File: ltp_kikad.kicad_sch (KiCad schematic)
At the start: 17 parts, among them IC1 SamacSys_Parts_HT16K33-28SOP, IC2 SamacSys_Parts_HT16K33-28SOP, J2 RPi_GPIO

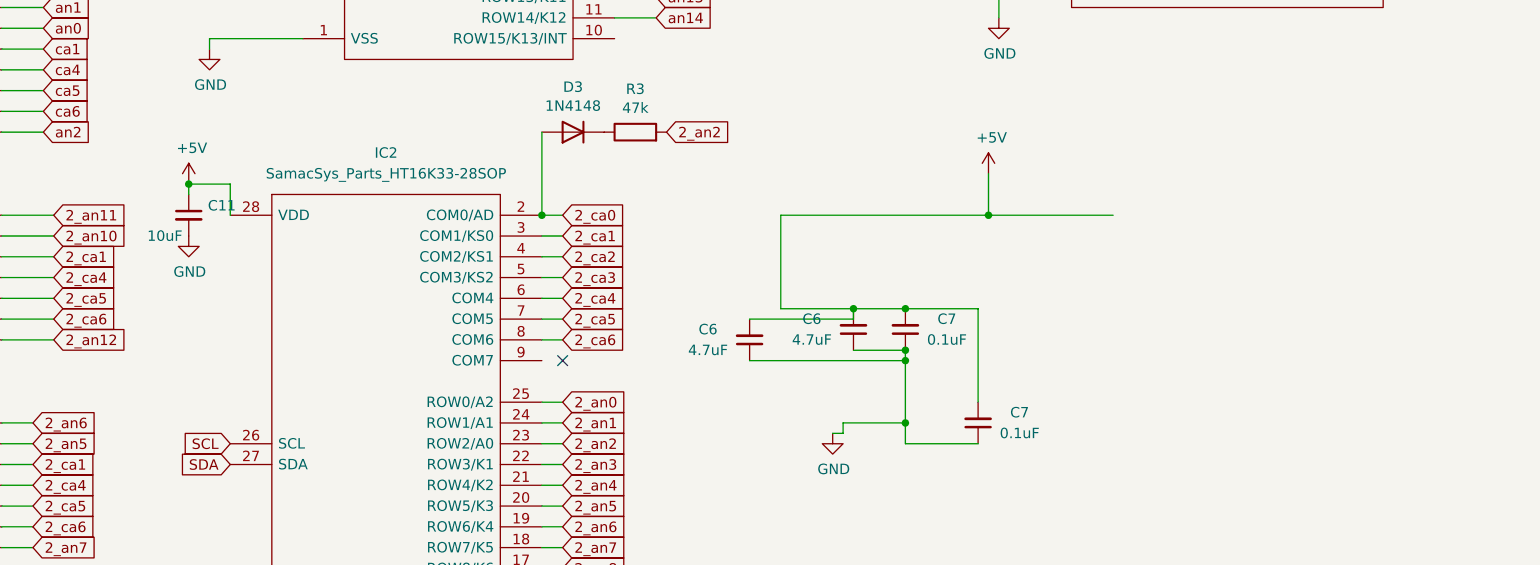
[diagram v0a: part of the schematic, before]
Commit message: Add bypas cap
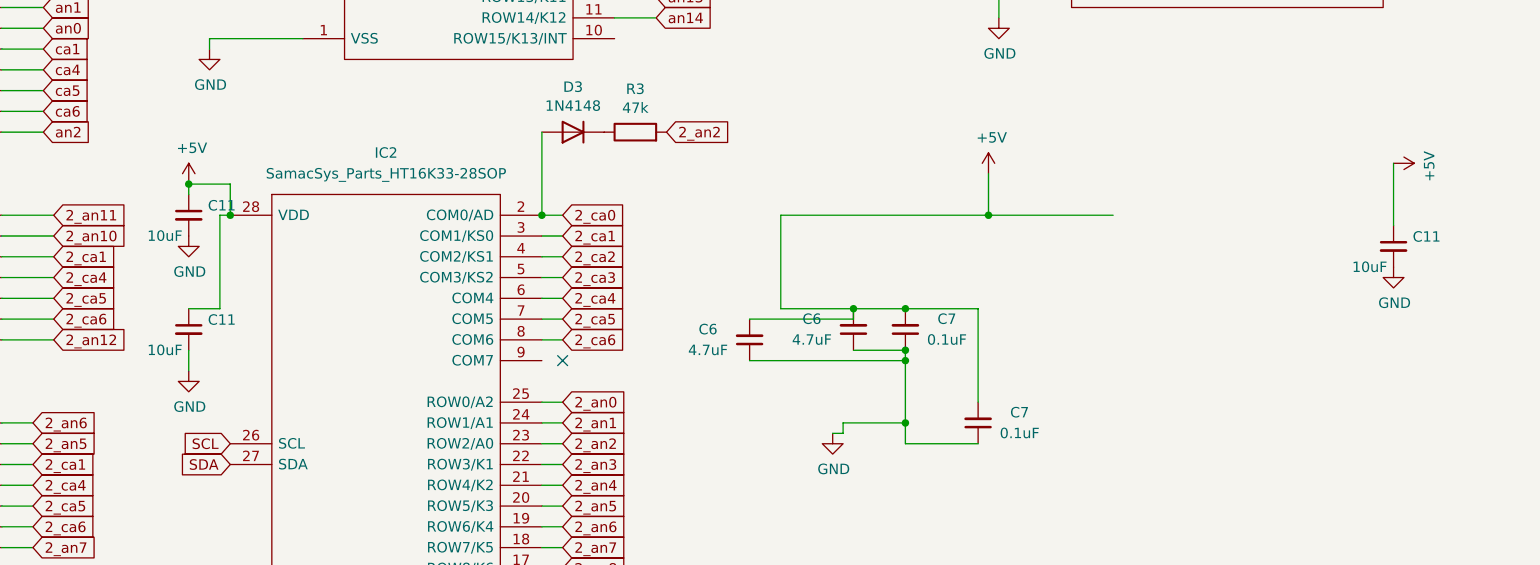
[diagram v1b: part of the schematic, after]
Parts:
- added C11 (x2): 10uF, Capacitor_SMD:C_0603_1608Metric, symbol Device:C_Small
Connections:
- net +5V: now also C11.1, C11.1
- net GND: now also C11.2, C11.2
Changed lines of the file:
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@@
   (junction (at 201.93 134.62) (diameter 0) (color 0 0 0 0)
+  )
+  (junction (at 119.38 118.11) (diameter 0) (color 0 0 0 0)
   )
   (junction (at 195.58 129.54) (diameter 0) (color 0 0 0 0)
@@
     (stroke (width 0) (type default))
   )
+  (wire (pts (xy 261.62 111.76) (xy 261.62 119.38))
+    (stroke (width 0) (type default))
+  )
   (wire (pts (xy 91.44 182.88) (xy 96.52 182.88))
     (stroke (width 0) (type default))
@@
     (stroke (width 0) (type default))
   )
+  (wire (pts (xy 118.11 118.11) (xy 119.38 118.11))
+    (stroke (width 0) (type default))
+  )
   (wire (pts (xy 91.44 170.18) (xy 96.52 170.18))
     (stroke (width 0) (type default))
@@
     (stroke (width 0) (type default))
   )
+  (wire (pts (xy 114.3 134.62) (xy 114.3 137.16))
+    (stroke (width 0) (type default))
+  )
   (wire (pts (xy 157.48 140.97) (xy 160.02 140.97))
     (stroke (width 0) (type default))
   )
+  (wire (pts (xy 118.11 118.11) (xy 118.11 129.54))
+    (stroke (width 0) (type default))
+  )
   (wire (pts (xy 24.13 102.87) (xy 30.48 102.87))
     (stroke (width 0) (type default))
@@
   )
   (wire (pts (xy 91.44 185.42) (xy 96.52 185.42))
+    (stroke (width 0) (type default))
+  )
+  (wire (pts (xy 118.11 129.54) (xy 114.3 129.54))
     (stroke (width 0) (type default))
   )
@@
         (path "/eed35b77-cbf9-4596-9b17-2558f81058ba"
           (reference "C2") (unit 1)
+        )
+      )
+    )
+  )
+  (symbol (lib_id "power:+5V") (at 261.62 111.76 270) (unit 1)
+    (in_bom yes) (on_board yes) (dnp no)
+    (property "Reference" "#PWR08" (at 257.81 111.76 0)
+      (effects (font (size 1.27 1.27)) hide)
+    )
+    (property "Value" "+5V" (at 266.0142 112.141 0)
+      (effects (font (size 1.27 1.27)))
+    )
+    (property "Footprint" "" (at 261.62 111.76 0)
+      (effects (font (size 1.27 1.27)) hide)
+    )
+    (property "Datasheet" "" (at 261.62 111.76 0)
+      (effects (font (size 1.27 1.27)) hide)
+    )
+    (pin "1")
+    (instances
+      (project "LTP305_ESP32_CLOCK"
+        (path "/c007e288-8439-49d9-bbdf-49724c34958c"
+          (reference "#PWR08") (unit 1)
+        )
+      )
+      (project "ltp_kikad"
+        (path "/eed35b77-cbf9-4596-9b17-2558f81058ba"
+          (reference "#PWR013") (unit 1)
+        )
+      )
+    )
+  )
+  (symbol (lib_id "power:GND") (at 114.3 137.16 0) (unit 1)
+    (in_bom yes) (on_board yes) (dnp no)
+    (property "Reference" "#PWR038" (at 114.3 143.51 0)
+      (effects (font (size 1.27 1.27)) hide)
+    )
+    (property "Value" "GND" (at 114.427 141.5542 0)
+      (effects (font (size 1.27 1.27)))
+    )
+    (property "Footprint" "" (at 114.3 137.16 0)
+      (effects (font (size 1.27 1.27)) hide)
+    )
+    (property "Datasheet" "" (at 114.3 137.16 0)
+      (effects (font (size 1.27 1.27)) hide)
+    )
+    (pin "1")
+    (instances
+      (project "LTP305_ESP32_CLOCK"
+        (path "/c007e288-8439-49d9-bbdf-49724c34958c"
+          (reference "#PWR038") (unit 1)
+        )
+      )
+      (project "ltp_kikad"
+        (path "/eed35b77-cbf9-4596-9b17-2558f81058ba"
+          (reference "#PWR012") (unit 1)
+        )
+      )
+    )
+  )
+  (symbol (lib_id "Device:C_Small") (at 114.3 132.08 0) (unit 1)
+    (in_bom yes) (on_board yes) (dnp no)
+    (property "Reference" "C11" (at 116.6368 130.9116 0)
+      (effects (font (size 1.27 1.27)) (justify left))
+    )
+    (property "Value" "10uF" (at 109.22 134.62 0)
+      (effects (font (size 1.27 1.27)) (justify left))
+    )
+    (property "Footprint" "Capacitor_SMD:C_0603_1608Metric" (at 114.3 132.08 0)
+      (effects (font (size 1.27 1.27)) hide)
+    )
+    (property "Datasheet" "~" (at 114.3 132.08 0)
+      (effects (font (size 1.27 1.27)) hide)
+    )
+    (pin "1")
+    (pin "2")
+    (instances
+      (project "LTP305_ESP32_CLOCK"
+        (path "/c007e288-8439-49d9-bbdf-49724c34958c"
+          (reference "C11") (unit 1)
+        )
+      )
+      (project "ltp_kikad"
+        (path "/eed35b77-cbf9-4596-9b17-2558f81058ba"
+          (reference "C7") (unit 1)
         )
       )
@@
         (path "/eed35b77-cbf9-4596-9b17-2558f81058ba"
           (reference "IC1") (unit 1)
+        )
+      )
+    )
+  )
+  (symbol (lib_id "Device:C_Small") (at 261.62 121.92 0) (unit 1)
+    (in_bom yes) (on_board yes) (dnp no)
+    (property "Reference" "C11" (at 263.9568 120.7516 0)
+      (effects (font (size 1.27 1.27)) (justify left))
+    )
+    (property "Value" "10uF" (at 256.54 124.46 0)
+      (effects (font (size 1.27 1.27)) (justify left))
+    )
+    (property "Footprint" "Capacitor_SMD:C_0603_1608Metric" (at 261.62 121.92 0)
+      (effects (font (size 1.27 1.27)) hide)
+    )
+    (property "Datasheet" "~" (at 261.62 121.92 0)
+      (effects (font (size 1.27 1.27)) hide)
+    )
+    (pin "1")
+    (pin "2")
+    (instances
+      (project "LTP305_ESP32_CLOCK"
+        (path "/c007e288-8439-49d9-bbdf-49724c34958c"
+          (reference "C11") (unit 1)
+        )
+      )
+      (project "ltp_kikad"
+        (path "/eed35b77-cbf9-4596-9b17-2558f81058ba"
+          (reference "C8") (unit 1)
         )
       )
@@
         )
       )
+    )
+  )
+  (symbol (lib_id "power:GND") (at 261.62 124.46 0) (unit 1)
+    (in_bom yes) (on_board yes) (dnp no)
+    (property "Reference" "#PWR038" (at 261.62 130.81 0)
+      (effects (font (size 1.27 1.27)) hide)
+    )
+    (property "Value" "GND" (at 261.747 128.8542 0)
+      (effects (font (size 1.27 1.27)))
+    )
+    (property "Footprint" "" (at 261.62 124.46 0)
+      (effects (font (size 1.27 1.27)) hide)
+    )
+    (property "Datasheet" "" (at 261.62 124.46 0)
+      (effects (font (size 1.27 1.27)) hide)
+    )
+    (pin "1")
+    (instances
+      (project "LTP305_ESP32_CLOCK"
+        (path "/c007e288-8439-49d9-bbdf-49724c34958c"
+          (reference "#PWR038") (unit 1)
+        )
+      )
+      (project "ltp_kikad"
+        (path "/eed35b77-cbf9-4596-9b17-2558f81058ba"
+          (reference "#PWR014") (unit 1)
+        )
+      )

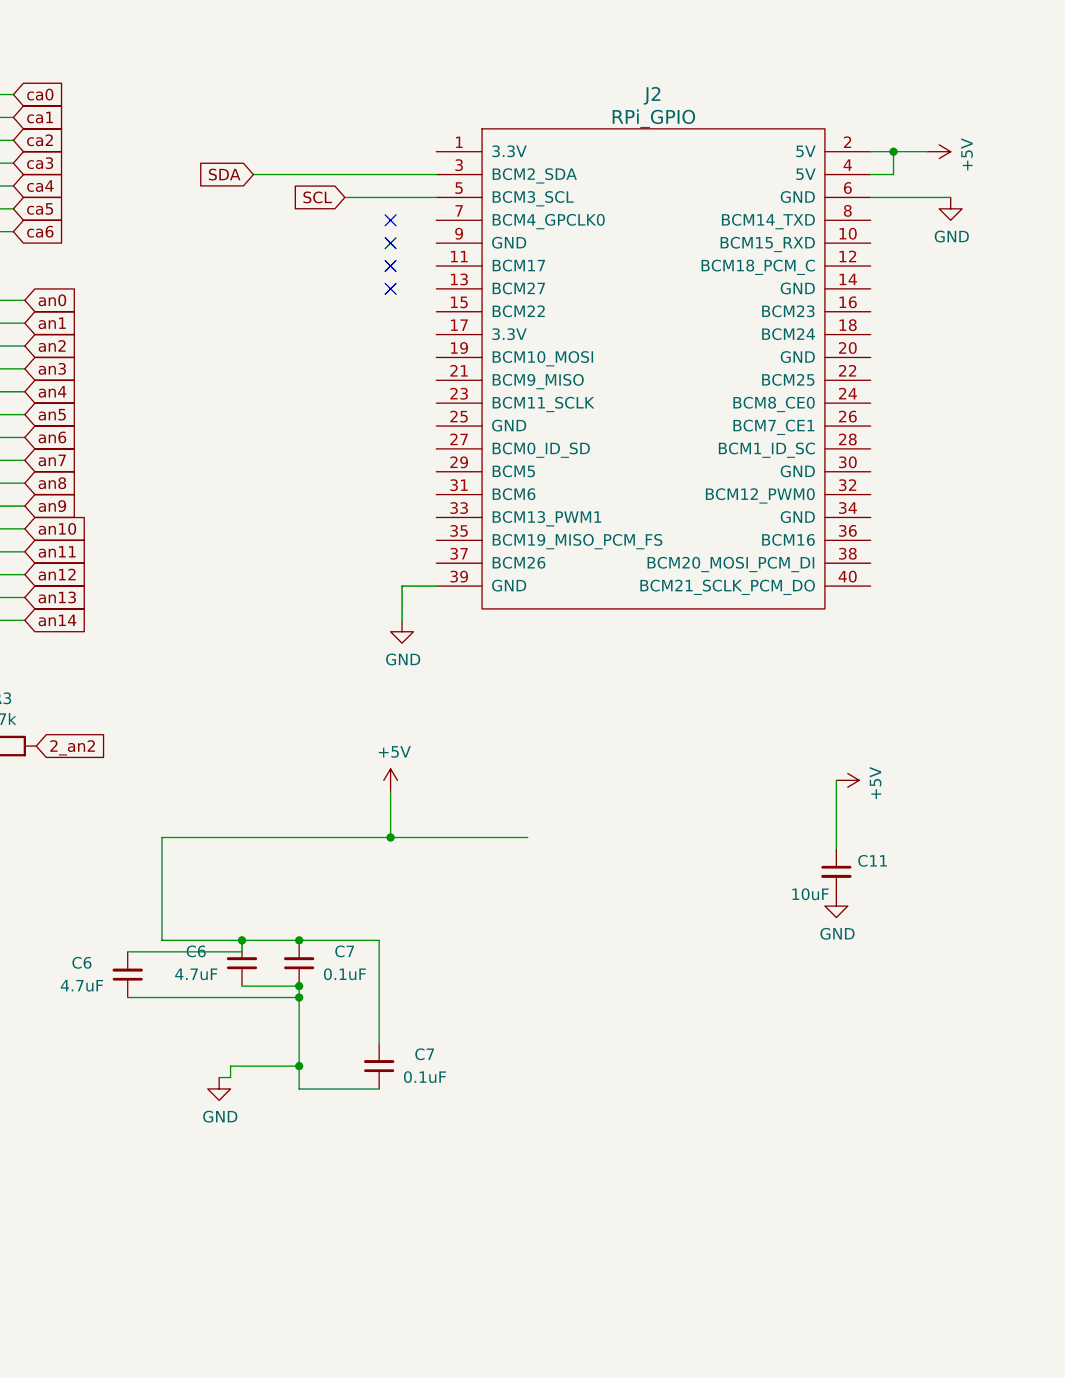
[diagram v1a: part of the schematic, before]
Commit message: Add qwiic stemma i2c connector
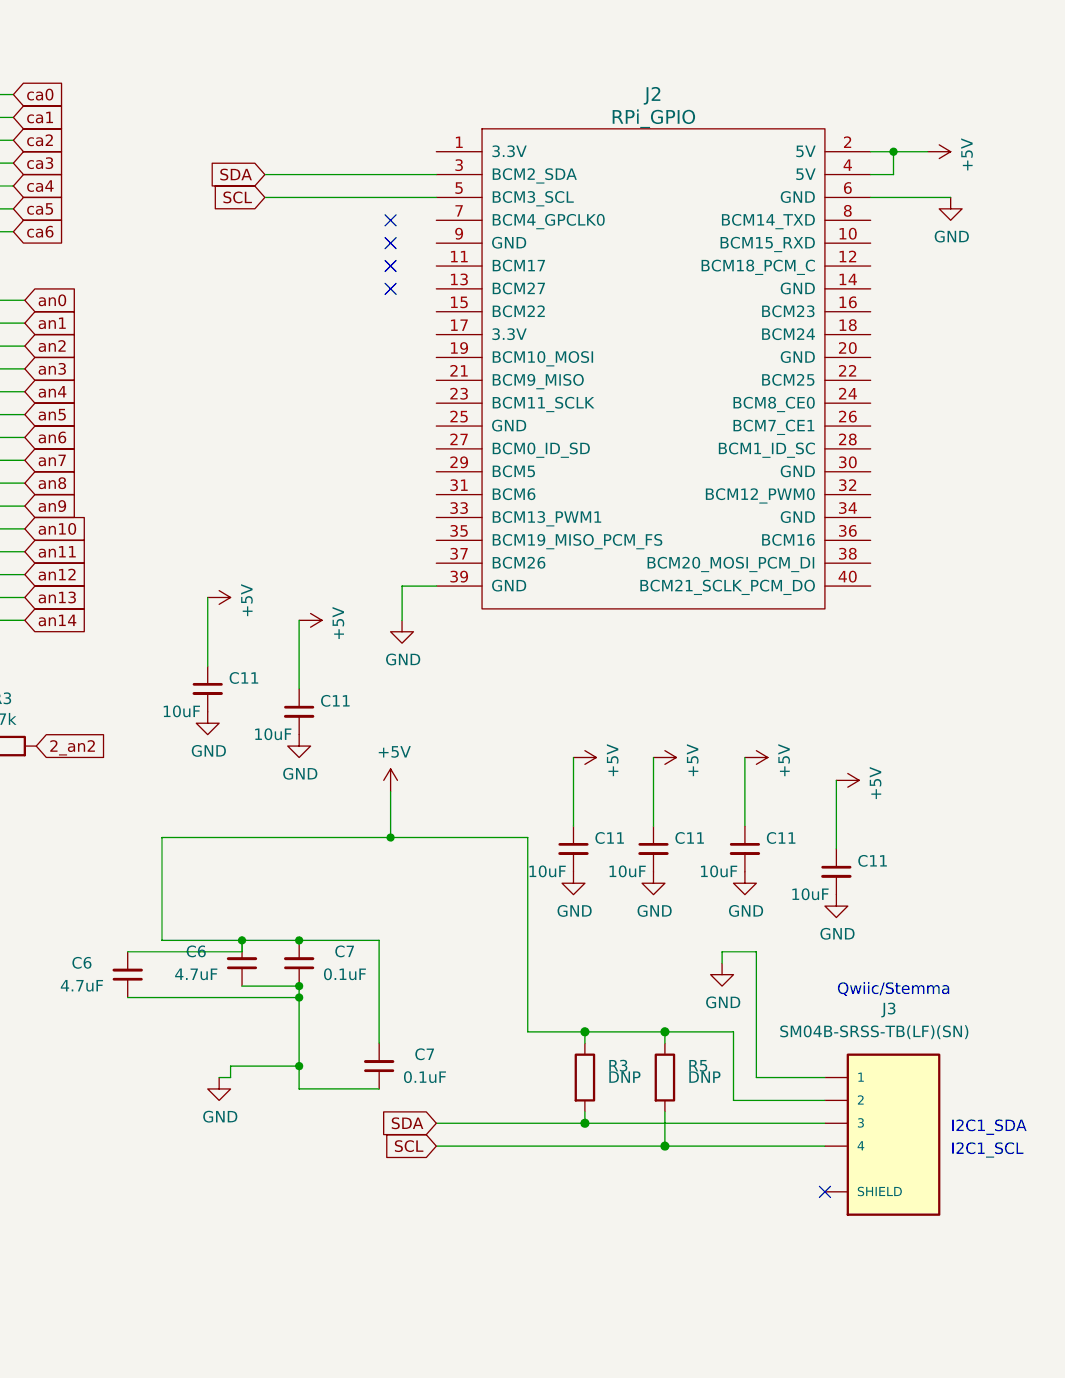
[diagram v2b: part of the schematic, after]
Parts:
- added C11 (x5): 10uF, Capacitor_SMD:C_0603_1608Metric, symbol Device:C_Small
- added J3: SM04B-SRSS-TB(LF)(SN), LTP-305G:JST_SM04B-SRSS-TB(LF)(SN), symbol SM04B-SRSS-TB_LF__SN_:SM04B-SRSS-TB(LF)(SN)
- added R3, R5: DNP, Resistor_SMD:R_0603_1608Metric_Pad0.98x0.95mm_HandSolder, symbol Device:R
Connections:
- net +5V: now also C11.1, C11.1, C11.1, C11.1, C11.1, J3.2, R3.1, R5.1
- net GND: now also C11.2, C11.2, C11.2, C11.2, C11.2, J3.1
- net SCL: now also J3.4, R5.2
- net SDA: now also J3.3, R3.2
- new net: J3.S1 (SHIELD), J3.S2 (SHIELD)
- no-connect marks 8 -> 9
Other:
- note added: "I2C1_SCL"
- note added: "I2C1_SDA"
- note added: "Qwiic/Stemma"

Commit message: Optimize design, add bypass caps
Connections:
- net GND: now also J3.S1 (SHIELD), J3.S2 (SHIELD)
- no-connect marks 9 -> 8
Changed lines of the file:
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@@
   (no_connect (at 160.02 135.89))
   (no_connect (at 26.67 130.81))
-  (no_connect (at 260.35 157.48))
   (wire (pts (xy 26.67 43.18) (xy 30.48 43.18))
     (stroke (width 0) (type default))
@@
     (stroke (width 0) (type default))
   )
+  (wire (pts (xy 260.35 157.48) (xy 255.27 157.48))
+    (stroke (width 0) (type default))
+  )
   (wire (pts (xy 157.48 125.73) (xy 160.02 125.73))
     (stroke (width 0) (type default))
@@
   )
   (wire (pts (xy 157.48 118.11) (xy 160.02 118.11))
+    (stroke (width 0) (type default))
+  )
+  (wire (pts (xy 255.27 157.48) (xy 255.27 158.75))
     (stroke (width 0) (type default))
   )
@@
         )
       )
+    )
+  )
+  (symbol (lib_id "power:GND") (at 255.27 158.75 0) (unit 1)
+    (in_bom yes) (on_board yes) (dnp no)
+    (property "Reference" "#PWR0109" (at 255.27 165.1 0)
+      (effects (font (size 1.27 1.27)) hide)
+    )
+    (property "Value" "GND" (at 255.397 163.1442 0)
+      (effects (font (size 1.27 1.27)))
+    )
+    (property "Footprint" "" (at 255.27 158.75 0)
+      (effects (font (size 1.27 1.27)) hide)
+    )
+    (property "Datasheet" "" (at 255.27 158.75 0)
+      (effects (font (size 1.27 1.27)) hide)
+    )
+    (pin "1")
+    (instances
+      (project "cm4-gpio"
+        (path "/9052c69d-def3-4232-bac1-59988fb85f45"
+          (reference "#PWR0109") (unit 1)
+        )
+      )
+      (project "ltp_kikad"
+        (path "/eed35b77-cbf9-4596-9b17-2558f81058ba"
+          (reference "#PWR026") (unit 1)
+        )
+      )
